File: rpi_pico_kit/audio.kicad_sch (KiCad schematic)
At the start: 36 parts, among them J10 AudioJack-CUI-SJ-3523-SMT, J11 AudioJack-CUI-SJ-3523-SMT, Q7 BSS138, U7 NC7WZ16P6X, U8 PCM5101A, U9 TLV70033_SOT23-5

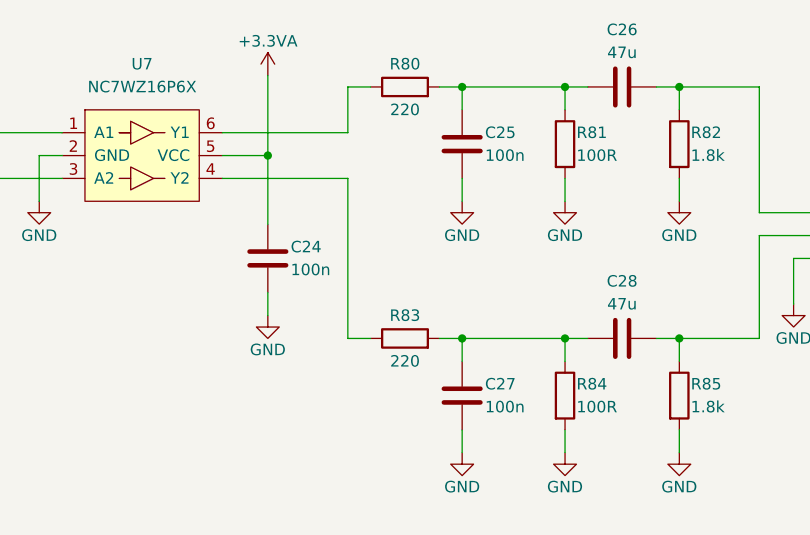
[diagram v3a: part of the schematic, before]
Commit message: added MPNs for resistors
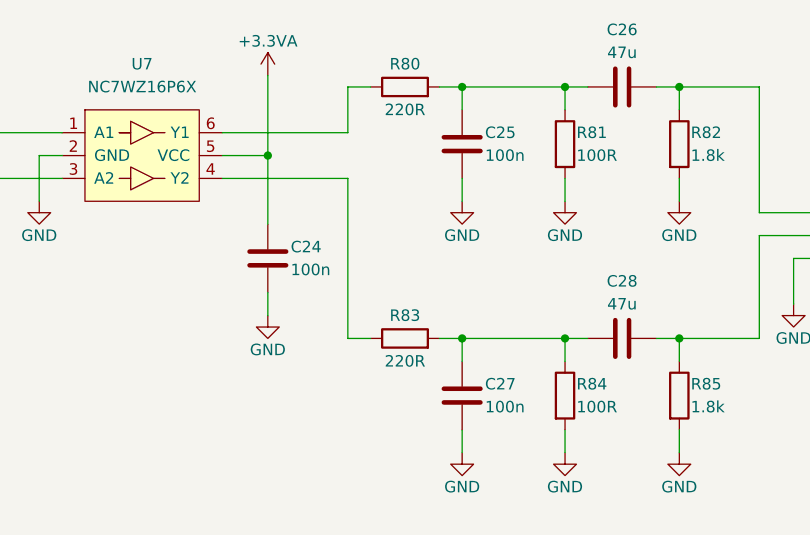
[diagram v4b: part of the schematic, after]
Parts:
- R80, R83: value 220 -> 220R; Manufacturer Part Number (none) -> RC0805FR-07220RL; Supplier (none) -> Digikey; Supplier Part URL (none) -> https://www.digikey.cz/en/products/detail/yageo/RC0805FR-07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
- R81, R84: Manufacturer Part Number (none) -> RC0805FR-07100RL; Supplier (none) -> Digikey; Supplier Part URL (none) -> https://www.digikey.cz/en/products/detail/yageo/RC0805FR-07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
- R82, R85: Manufacturer Part Number (none) -> RC0805FR-071K8L; Supplier (none) -> Digikey; Supplier Part URL (none) -> https://www.digikey.cz/en/products/detail/yageo/RC0805FR-07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
- R86, R87: Manufacturer Part Number (none) -> RC0805FR-07470RL; Supplier (none) -> Digikey; Supplier Part URL (none) -> https://www.digikey.cz/en/products/detail/yageo/RC0805FR-07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
- R88: Manufacturer Part Number (none) -> RC0805FR-071KL; Supplier (none) -> Digikey; Supplier Part URL (none) -> https://www.digikey.cz/en/products/detail/yageo/RC0805FR-07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
- R89: Manufacturer Part Number (none) -> RC0805FR-0710KL; Supplier (none) -> Digikey; Supplier Part URL (none) -> https://www.digikey.cz/en/products/detail/yageo/RC0805FR-07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
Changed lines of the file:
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@@
+      (effects (font (size 1.27 1.27)) hide)
+    )
+    (property "Manufacturer Part Number" "RC0805FR-071K8L" (id 4) (at 113.03 39.37 0)
+      (effects (font (size 1.27 1.27)) hide)
+    )
+    (property "Supplier" "Digikey" (id 5) (at 113.03 39.37 0)
+      (effects (font (size 1.27 1.27)) hide)
+    )
+    (property "Supplier Part URL" "https://www.digikey.cz/en/products/detail/yageo/RC0805FR-071K8L/727520" (id 6) (at 113.03 39.37 0)
       (effects (font (size 1.27 1.27)) hide)
     )
@@
     )
     (property "Datasheet" "~" (id 3) (at 205.74 114.3 0)
+      (effects (font (size 1.27 1.27)) hide)
+    )
+    (property "Manufacturer Part Number" "RC0805FR-071KL" (id 4) (at 205.74 114.3 0)
+      (effects (font (size 1.27 1.27)) hide)
+    )
+    (property "Supplier Part URL" "https://www.digikey.cz/en/products/detail/yageo/RC0805FR-071KL/727444" (id 5) (at 205.74 114.3 0)
+      (effects (font (size 1.27 1.27)) hide)
+    )
+    (property "Supplier" "Digikey" (id 6) (at 205.74 114.3 0)
       (effects (font (size 1.27 1.27)) hide)
     )
@@
       (effects (font (size 1.27 1.27)))
     )
-    (property "Value" "220" (id 1) (at 82.55 35.56 90)
+    (property "Value" "220R" (id 1) (at 82.55 35.56 90)
       (effects (font (size 1.27 1.27)))
     )
@@
     )
     (property "Datasheet" "~" (id 3) (at 82.55 33.02 0)
+      (effects (font (size 1.27 1.27)) hide)
+    )
+    (property "Manufacturer Part Number" "RC0805FR-07220RL" (id 4) (at 82.55 33.02 0)
+      (effects (font (size 1.27 1.27)) hide)
+    )
+    (property "Supplier" "Digikey" (id 5) (at 82.55 33.02 0)
+      (effects (font (size 1.27 1.27)) hide)
+    )
+    (property "Supplier Part URL" "https://www.digikey.cz/en/products/detail/yageo/RC0805FR-07220RL/727741" (id 6) (at 82.55 33.02 0)
       (effects (font (size 1.27 1.27)) hide)
     )
@@
       (effects (font (size 1.27 1.27)) hide)
     )
+    (property "Manufacturer Part Number" "RC0805FR-07470RL" (id 4) (at 99.06 132.08 0)
+      (effects (font (size 1.27 1.27)) hide)
+    )
+    (property "Supplier Part URL" "https://www.digikey.cz/en/products/detail/yageo/RC0805FR-07470RL/727976" (id 5) (at 99.06 132.08 0)
+      (effects (font (size 1.27 1.27)) hide)
+    )
+    (property "Supplier" "Digikey" (id 6) (at 99.06 132.08 0)
+      (effects (font (size 1.27 1.27)) hide)
+    )
     (pin "1")
     (pin "2")
@@
       (effects (font (size 1.27 1.27)) hide)
     )
+    (property "Manufacturer Part Number" "RC0805FR-071K8L" (id 4) (at 113.03 67.31 0)
+      (effects (font (size 1.27 1.27)) hide)
+    )
+    (property "Supplier" "Digikey" (id 5) (at 113.03 67.31 0)
+      (effects (font (size 1.27 1.27)) hide)
+    )
+    (property "Supplier Part URL" "https://www.digikey.cz/en/products/detail/yageo/RC0805FR-071K8L/727520" (id 6) (at 113.03 67.31 0)
+      (effects (font (size 1.27 1.27)) hide)
+    )
     (pin "1")
     (pin "2")
@@
       (effects (font (size 1.27 1.27)) hide)
     )
+    (property "Manufacturer Part Number" "RC0805FR-0710KL" (id 4) (at 229.87 120.65 0)
+      (effects (font (size 1.27 1.27)) hide)
+    )
+    (property "Supplier Part URL" "https://www.digikey.cz/en/products/detail/yageo/RC0805FR-0710KL/727535" (id 5) (at 229.87 120.65 0)
+      (effects (font (size 1.27 1.27)) hide)
+    )
+    (property "Supplier" "Digikey" (id 6) (at 229.87 120.65 0)
+      (effects (font (size 1.27 1.27)) hide)
+    )
     (pin "1")
     (pin "2")
@@
       (effects (font (size 1.27 1.27)) hide)
     )
+    (property "Manufacturer Part Number" "RC0805FR-07100RL" (id 4) (at 100.33 67.31 0)
+      (effects (font (size 1.27 1.27)) hide)
+    )
+    (property "Supplier Part URL" "https://www.digikey.cz/en/products/detail/yageo/RC0805FR-07100RL/727543" (id 5) (at 100.33 67.31 0)
+      (effects (font (size 1.27 1.27)) hide)
+    )
+    (property "Supplier" "Digikey" (id 6) (at 100.33 67.31 0)
+      (effects (font (size 1.27 1.27)) hide)
+    )
     (pin "1")
     (pin "2")
@@
     )
     (property "Datasheet" "~" (id 3) (at 99.06 138.43 0)
+      (effects (font (size 1.27 1.27)) hide)
+    )
+    (property "Manufacturer Part Number" "RC0805FR-07470RL" (id 4) (at 99.06 138.43 0)
+      (effects (font (size 1.27 1.27)) hide)
+    )
+    (property "Supplier Part URL" "https://www.digikey.cz/en/products/detail/yageo/RC0805FR-07470RL/727976" (id 5) (at 99.06 138.43 0)
+      (effects (font (size 1.27 1.27)) hide)
+    )
+    (property "Supplier" "Digikey" (id 6) (at 99.06 138.43 0)
       (effects (font (size 1.27 1.27)) hide)
     )
@@
       (effects (font (size 1.27 1.27)))
     )
-    (property "Value" "220" (id 1) (at 82.55 63.5 90)
+    (property "Value" "220R" (id 1) (at 82.55 63.5 90)
       (effects (font (size 1.27 1.27)))
     )
@@
     )
     (property "Datasheet" "~" (id 3) (at 82.55 60.96 0)
+      (effects (font (size 1.27 1.27)) hide)
+    )
+    (property "Manufacturer Part Number" "RC0805FR-07220RL" (id 4) (at 82.55 60.96 0)
+      (effects (font (size 1.27 1.27)) hide)
+    )
+    (property "Supplier" "Digikey" (id 5) (at 82.55 60.96 0)
+      (effects (font (size 1.27 1.27)) hide)
+    )
+    (property "Supplier Part URL" "https://www.digikey.cz/en/products/detail/yageo/RC0805FR-07220RL/727741" (id 6) (at 82.55 60.96 0)
       (effects (font (size 1.27 1.27)) hide)
     )
@@
       (effects (font (size 1.27 1.27)) hide)
     )
+    (property "Manufacturer Part Number" "RC0805FR-07100RL" (id 4) (at 100.33 39.37 0)
+      (effects (font (size 1.27 1.27)) hide)
+    )
+    (property "Supplier Part URL" "https://www.digikey.cz/en/products/detail/yageo/RC0805FR-07100RL/727543" (id 5) (at 100.33 39.37 0)
+      (effects (font (size 1.27 1.27)) hide)
+    )
+    (property "Supplier" "Digikey" (id 6) (at 100.33 39.37 0)
+      (effects (font (size 1.27 1.27)) hide)
+    )

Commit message: little changes
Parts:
- JP2: footprint TestPoint:TestPoint_2Pads_Pitch2.54mm_Drill0.8mm -> Connector_PinHeader_2.54mm:PinHeader_1x02_P2.54mm_Vertical
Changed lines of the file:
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@@
       (effects (font (size 1.27 1.27)))
     )
-    (property "Footprint" "TestPoint:TestPoint_2Pads_Pitch2.54mm_Drill0.8mm" (id 2) (at 219.71 114.3 0)
+    (property "Footprint" "Connector_PinHeader_2.54mm:PinHeader_1x02_P2.54mm_Vertical" (id 2) (at 219.71 114.3 0)
       (effects (font (size 1.27 1.27)) hide)
     )
@@
       (effects (font (size 1.27 1.27)) hide)
     )
-    (property "Datasheet" "" (id 3) (at 133.35 49.53 0)
+    (property "Datasheet" "~" (id 3) (at 133.35 49.53 0)
       (effects (font (size 1.27 1.27)) hide)
     )
@@
       (effects (font (size 1.27 1.27)) hide)
     )
-    (property "Datasheet" "" (id 3) (at 144.78 134.62 0)
-      (effects (font (size 1.27 1.27)) hide)
-    )
+    (property "Datasheet" "~" (id 3) (at 144.78 134.62 0)
+      (effects (font (size 1.27 1.27)) hide)
+    )

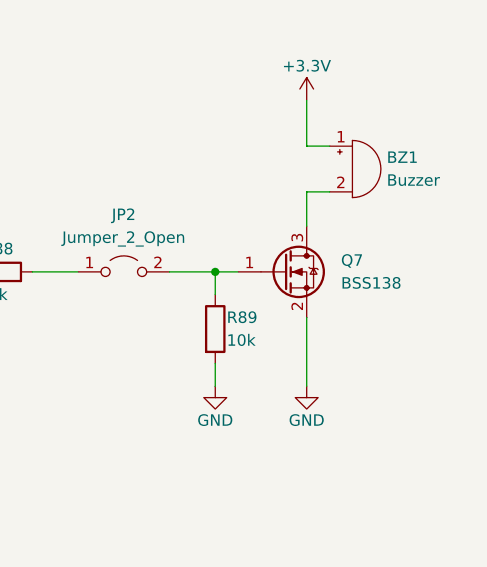
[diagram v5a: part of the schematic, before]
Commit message: added another MPNs, edited color of LEDs
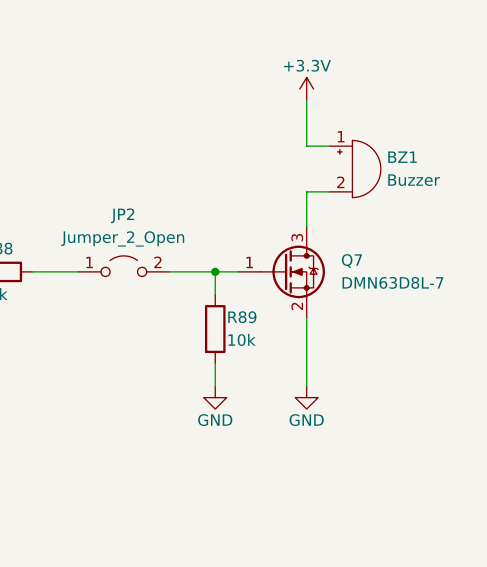
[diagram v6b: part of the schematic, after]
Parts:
- JP2: Manufacturer Part Number (none) -> PinHeader_1x02
- Q7: value BSS138 -> DMN63D8L-7; Manufacturer Part Number (none) -> DMN63D8L-7; Supplier (none) -> Digikey; Supplier Part URL (none) -> https://www.digikey.cz/en/products/detail/diodes-incorporat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
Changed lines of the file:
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@@
+      (effects (font (size 1.27 1.27)) hide)
+    )
+    (property "Manufacturer Part Number" "PinHeader_1x02" (id 4) (at 219.71 114.3 0)
       (effects (font (size 1.27 1.27)) hide)
     )
@@
       (effects (font (size 1.27 1.27)) hide)
     )
-    (property "Datasheet" "" (id 3) (at 53.34 40.64 0)
+    (property "Datasheet" "~" (id 3) (at 53.34 40.64 0)
       (effects (font (size 1.27 1.27)) hide)
     )
@@
       (effects (font (size 1.27 1.27)) (justify left))
     )
-    (property "Value" "BSS138" (id 1) (at 243.84 115.5699 0)
+    (property "Value" "DMN63D8L-7" (id 1) (at 243.84 115.5699 0)
       (effects (font (size 1.27 1.27)) (justify left))
     )
@@
       (effects (font (size 1.27 1.27)) (justify left) hide)
     )
-    (pin "1")
+    (property "Manufacturer Part Number" "DMN63D8L-7" (id 4) (at 237.49 114.3 0)
+      (effects (font (size 1.27 1.27)) hide)
+    )
+    (property "Supplier" "Digikey" (id 5) (at 237.49 114.3 0)
+      (effects (font (size 1.27 1.27)) hide)
+    )
+    (property "Supplier Part URL" "https://www.digikey.cz/en/products/detail/diodes-incorporated/DMN63D8L-7/5699705" (id 6) (at 237.49 114.3 0)
+      (effects (font (size 1.27 1.27)) hide)
+    )
+    (pin "1")

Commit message: added MPNs
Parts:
- JP2: Supplier (none) -> me
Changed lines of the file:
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@@
+      (effects (font (size 1.27 1.27)) hide)
+    )
+    (property "Supplier" "me" (id 5) (at 219.71 114.3 0)
       (effects (font (size 1.27 1.27)) hide)
     )
